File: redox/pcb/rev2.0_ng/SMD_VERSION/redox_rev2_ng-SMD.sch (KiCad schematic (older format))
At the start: 147 parts, among them J2 OLED-SSD1306, K1 KEYSW, K10 KEYSW, K11 KEYSW, K12 KEYSW, K13 KEYSW, K14 KEYSW, K15 KEYSW, K16 KEYSW, K17 KEYSW, K18 KEYSW, K19 KEYSW, K2 KEYSW, K20 KEYSW, K21 KEYSW, K22 KEYSW, K23 KEYSW, K24 KEYSW, K25 KEYSW, K26 KEYSW, K27 KEYSW, K28 KEYSW, K29 KEYSW, K3 KEYSW, K30 KEYSW, K31 KEYSW, K32 KEYSW, K33 KEYSW, K34 KEYSW, K35 KEYSW, K4 KEYSW, K5 KEYSW, K6 KEYSW, K7 KEYSW, K8 KEYSW, K9 KEYSW, P1 TC2030-AVR, Q1 2N7002, U1 PRTR5V0U2X, U2 ATmega32U4, Y1 16Mhz

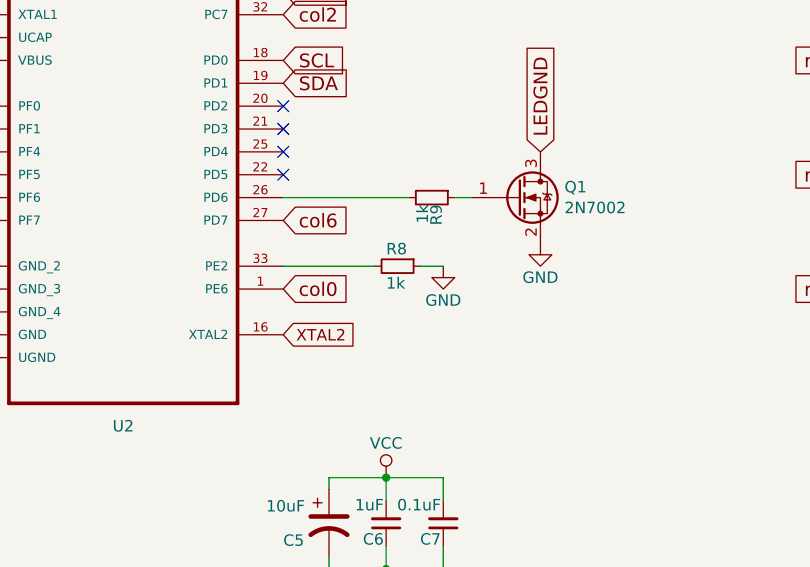
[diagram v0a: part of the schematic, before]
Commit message: Change PCB holes placement, TRSS connector, add JLC id.
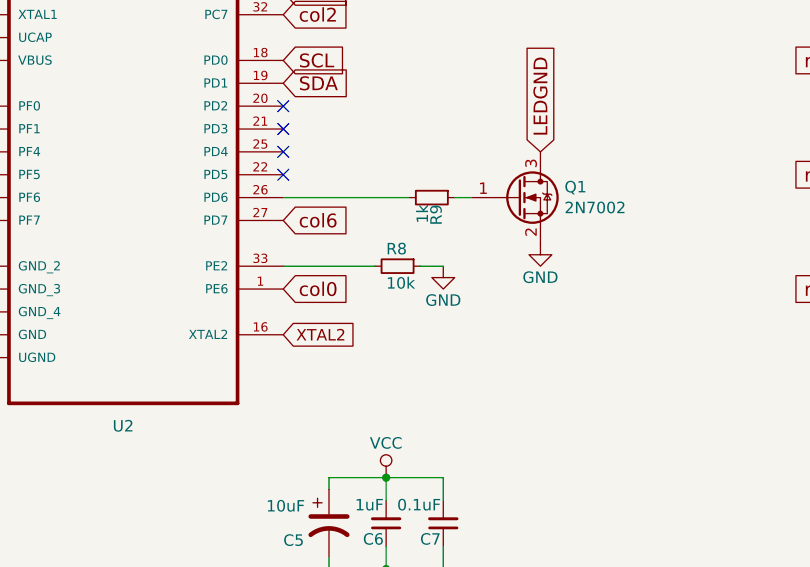
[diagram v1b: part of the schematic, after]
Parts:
- R8: value 1k -> 10k
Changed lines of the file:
@@
 AR Path="/5EDAEC91" Ref="R8"  Part="1"
 F 0 "R8" V 4600 3175 50  0000 L CNN
-F 1 "1k" V 4750 3175 50  0000 L CNN
+F 1 "10k" V 4750 3175 50  0000 L CNN
 F 2 "Keebio-Parts:R_0603" H 4675 3225 50  0001 C CNN
 F 3 "" H 4675 3225 50  0001 C CNN
